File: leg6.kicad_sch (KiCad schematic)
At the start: 12 parts, among them J17 Leg6 Motor1, J18 Leg16Motor2, J19 Leg6 Motor3

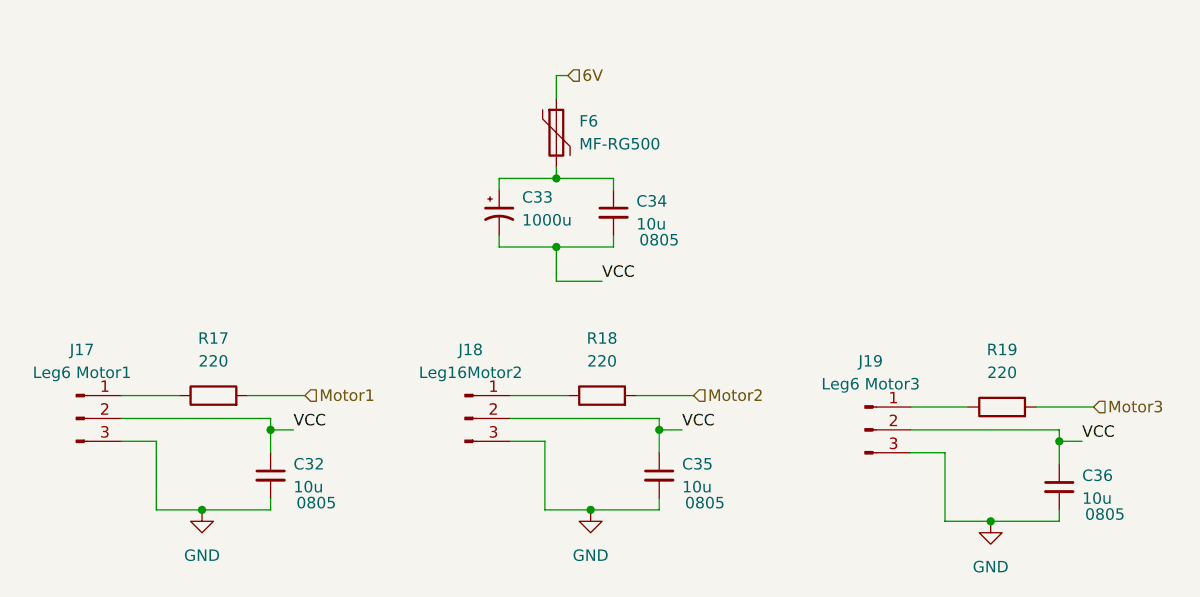
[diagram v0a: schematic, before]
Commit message: removed crystal, fixed caps
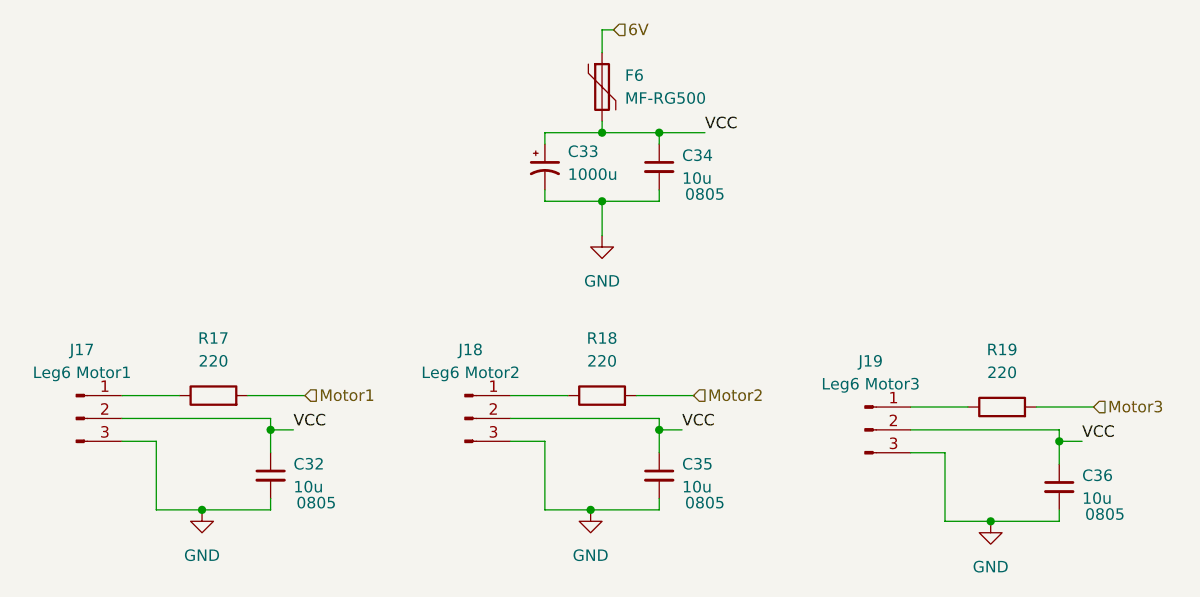
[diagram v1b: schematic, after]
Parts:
- J18: value Leg16Motor2 -> Leg6 Motor2
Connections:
- net GND: now also C33.2, C34.2
- net VCC: now also C33.1, C34.1, F6.2; no longer C33.2, C34.2
